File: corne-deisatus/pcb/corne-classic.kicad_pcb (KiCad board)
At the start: 2 copper layers, 147.2 x 94.7 mm, 101 parts, among them J1 MJ-4PP-9, J2 OLED, J3 LED, P1 i2c-pin, P2 i2c-pin, SW1 SW_PUSH, SW10 SW_PUSH, SW11 SW_PUSH, SW12 SW_PUSH, SW13 SW_PUSH, SW14 SW_PUSH, SW15 SW_PUSH, SW16 SW_PUSH, SW17 SW_PUSH, SW18 SW_PUSH, SW19 SW_PUSH, SW2 SW_PUSH, SW20 SW_PUSH, SW21 SW_PUSH, SW22 SW_PUSH, SW3 SW_PUSH, SW4 SW_PUSH, SW5 SW_PUSH, SW6 SW_PUSH, SW7 SW_PUSH, SW8 SW_PUSH, SW9 SW_PUSH, U1 ProMicro

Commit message: working on tracks
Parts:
- SW1, SW10, SW11, SW12, SW13, SW14, SW15, SW16, SW17, SW18, SW19, SW2, SW20, SW3, SW4, SW5, SW6, SW7, SW8, SW9: footprint kailh-pg1425-x-switch:MX-ALPS-Choc-X-straight-crane -> kailh-pg1425-x-switch:MX-ALPS-Choc-X-straight-crane2
- SW21, SW22: footprint kailh-pg1425-x-switch:MX-ALPS-Choc-X-straight-crane-u1.5 -> kailh-pg1425-x-switch:MX-ALPS-Choc-X-straight-crane2-u1.5
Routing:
- net GND: track 764.2 -> 76.1 mm, vias 43 -> 3
- net col1: track 221.3 -> 30.0 mm, vias 4 -> 2
- net col2: track 197.5 -> 17.9 mm, vias 8 -> 2
- net row0: track 205.5 -> 28.9 mm, vias 3 -> 0
- net col3: track 189.0 -> 17.6 mm, vias 6 -> 2
- net row1: track 191.7 -> 21.7 mm, vias 11 -> 0
- net col0: track 245.7 -> 95.9 mm, vias 4 -> 2
- net col4: track 161.0 -> 28.2 mm, vias 6 -> 2
- net Net-(L15-Pad3): track 77.2 -> 0.00 mm, vias 8 -> 0
- net col5: track 151.0 -> 77.2 mm, vias 2 -> 4
- net Net-(L14-Pad3): track 65.8 -> 0.00 mm, vias 8 -> 0
- net Net-(L4-Pad1): track 52.1 -> 0.00 mm, vias 5 -> 0
- net Net-(L2-Pad3): track 48.0 -> 0.00 mm, vias 3 -> 0
- net Net-(L1-Pad3): track 46.7 -> 0.00 mm, vias 3 -> 0
- net Net-(L5-Pad1): track 45.8 -> 0.00 mm, vias 3 -> 0
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- added copper zone on B.Cu, net GND

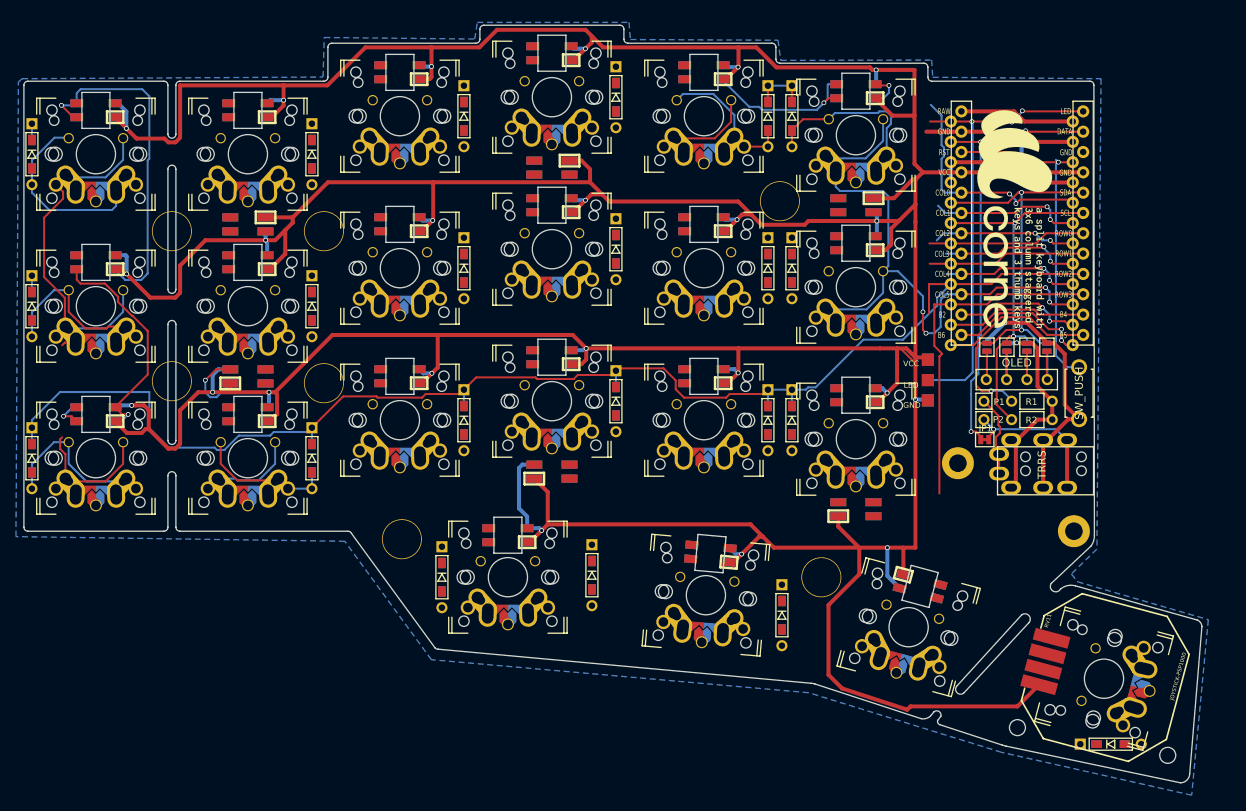
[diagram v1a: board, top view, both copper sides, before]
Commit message: adding tracks
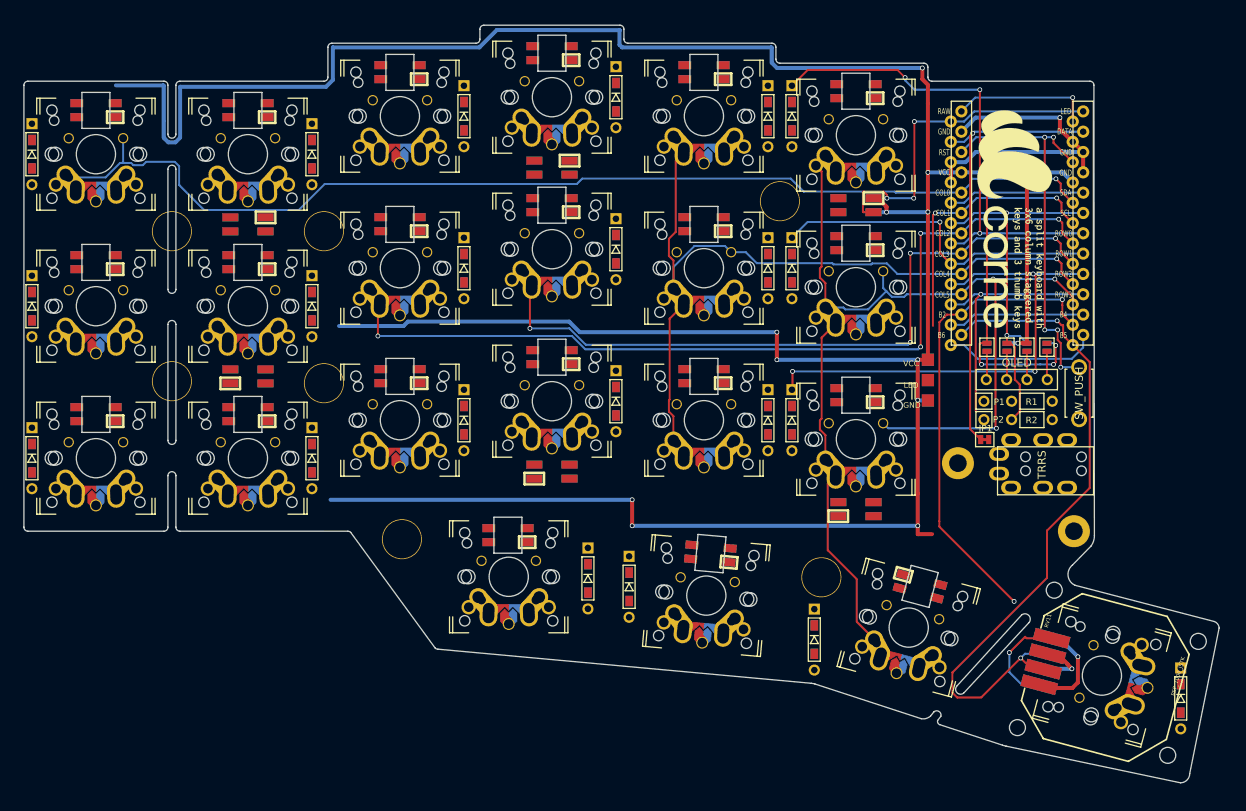
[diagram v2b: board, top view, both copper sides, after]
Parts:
- RV11: value JOYSTICK-PSP1000 -> PSP_1000_JSTK; footprint HackPack_Footprints:JOYSTICK-PSP1000 -> HackPack_Footprints:JOYSTICK-PSP1000-reverse
- SW20: footprint kailh-pg1425-x-switch:MX-ALPS-Choc-X-straight-crane2 -> kailh-pg1425-x-switch:MX-ALPS-Choc-X-straight-crane2-u1.5
- SW22: footprint kailh-pg1425-x-switch:MX-ALPS-Choc-X-straight-crane2-u1.5 -> kailh-pg1425-x-switch:MX-ALPS-Choc-X-straight-crane2
- moved SW19 75.5 mm to (121.6, 129.9), turned to 180 degrees
- moved D22 68.6 mm to (131.5, 130.2), turned to 270 degrees
- moved D21 50.9 mm to (205.6, 145.2)
- moved D20 28.9 mm to (159.8, 137.8)
- moved SW21 25.7 mm to (171.6, 136.3), turned to 165 degrees
- moved SW20 24.9 mm to (146.3, 132.3), turned to 175 degrees
- moved SW22 24.9 mm to (195.8, 142.3), turned to 255 degrees
- moved D19 23.4 mm to (136.7, 131.2)
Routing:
- net VCC: track 738.2 -> 404.4 mm, vias 24 -> 14
- net row2: track 172.1 -> 62.3 mm, vias 0 -> 3
- net col2: track 17.9 -> 108.6 mm, vias 2 -> 4
- net col3: track 17.6 -> 88.9 mm, vias 2 -> 4
- net analogY: track 17.5 -> 88.0 mm
- net col4: track 28.2 -> 94.0 mm, vias 2 -> 1
- net analogX: track 16.0 -> 72.7 mm, vias 2 -> 3
- net col5: track 77.2 -> 130.9 mm, vias 4 -> 3
- net col0: track 95.9 -> 138.6 mm, vias 2 -> 1
- net Net-(L13-Pad3): track 42.7 -> 0.00 mm, vias 1 -> 0
- net row0: track 28.9 -> 60.5 mm, vias 0 -> 3
- net Net-(L13-Pad1): track 28.5 -> 0.00 mm, vias 1 -> 0
- net Net-(D1-Pad2): track 28.3 -> 0.00 mm
- net GND: track 76.1 -> 48.2 mm, vias 3 -> 2
- net Net-(D6-Pad2): track 22.6 -> 0.00 mm
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- removed copper zone on B.Cu, net GND
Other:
- board size 147.2 x 94.7 mm -> 149.4 x 94.7 mm

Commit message: adding tracks
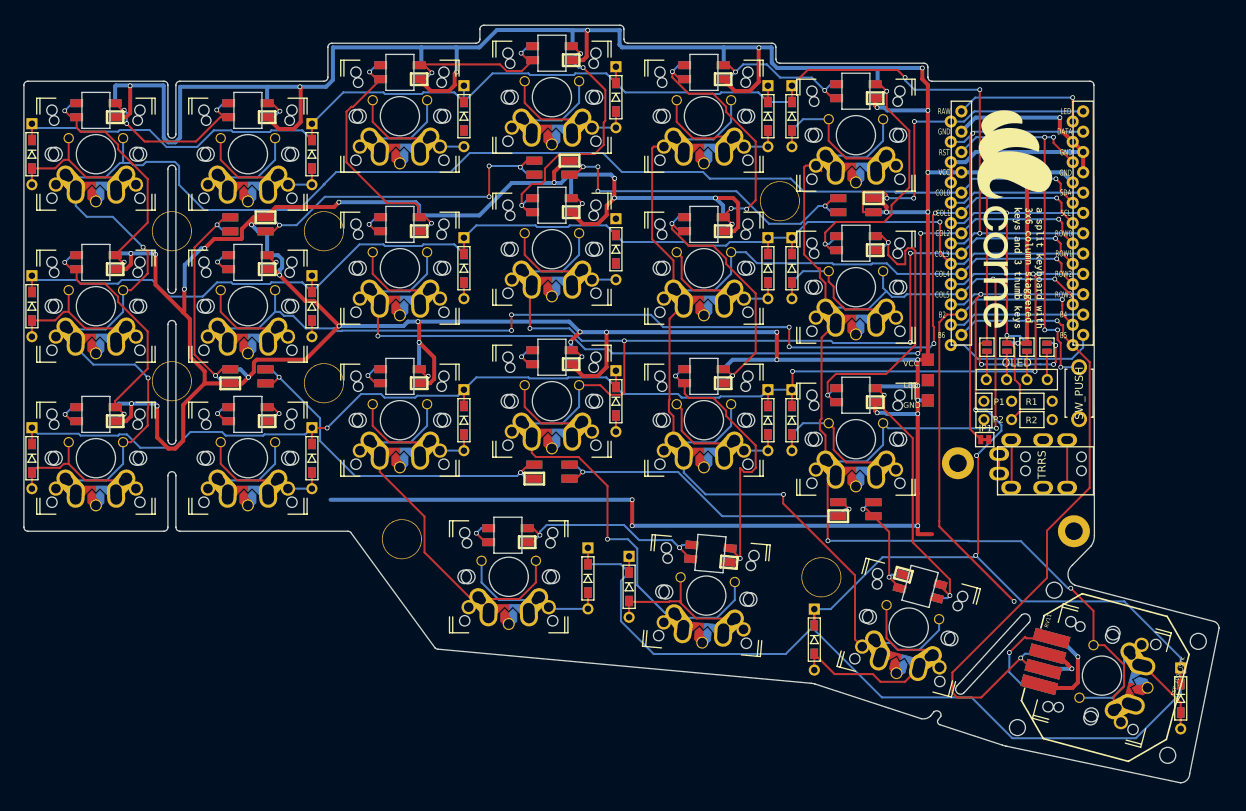
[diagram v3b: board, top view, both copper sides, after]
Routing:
- net VCC: track 404.4 -> 726.2 mm, vias 14 -> 44
- net row3: track 31.9 -> 214.1 mm, vias 1 -> 4
- net col1: track 34.1 -> 157.2 mm, vias 2 -> 7
- net row0: track 60.5 -> 176.2 mm
- net row2: track 62.3 -> 176.6 mm, vias 3 -> 4
- net row1: track 42.2 -> 155.6 mm
- net col3: track 88.9 -> 179.1 mm, vias 4 -> 6
- net col4: track 94.0 -> 166.4 mm, vias 1 -> 2
- net col2: track 108.6 -> 175.7 mm
- net col0: track 138.6 -> 203.9 mm, vias 1 -> 3
- net col5: track 130.9 -> 193.1 mm, vias 3 -> 5
- net Net-(L4-Pad1): track 0.00 -> 45.5 mm, vias 0 -> 2
- net Net-(L2-Pad3): track 0.77 -> 44.8 mm, vias 0 -> 4
- net Net-(L1-Pad3): track 0.00 -> 43.9 mm, vias 0 -> 4
- net Net-(L5-Pad1): track 0.00 -> 41.7 mm, vias 0 -> 2
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
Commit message: mostly done
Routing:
- net VCC: track 726.2 -> 809.8 mm, vias 44 -> 55
- net Net-(L15-Pad1): track 7.42 -> 32.4 mm
- net col1: track 157.2 -> 177.4 mm, vias 7 -> 8
- net analogX: track 72.7 -> 79.0 mm, vias 3 -> 5
- net Net-(L20-Pad3): track 7.65 -> 8.21 mm

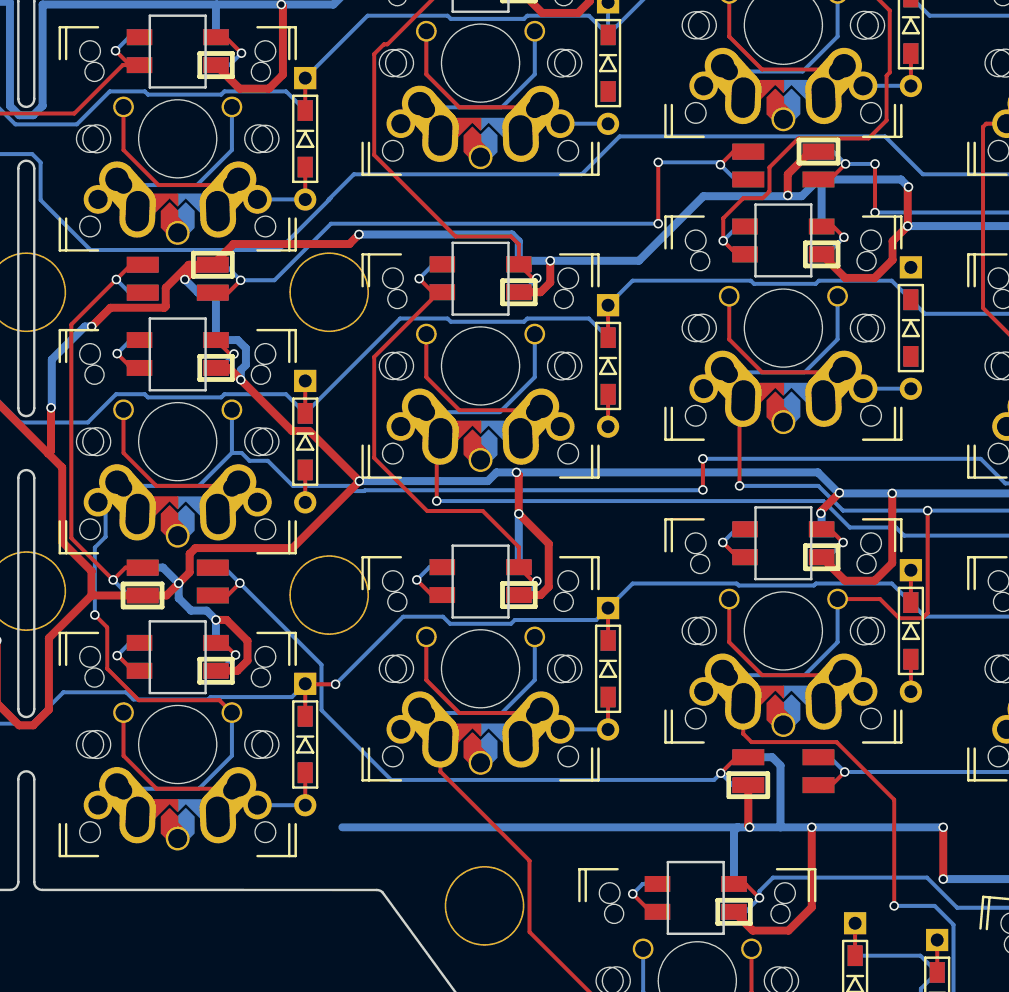
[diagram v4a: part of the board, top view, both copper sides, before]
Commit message: added all tracks except GND
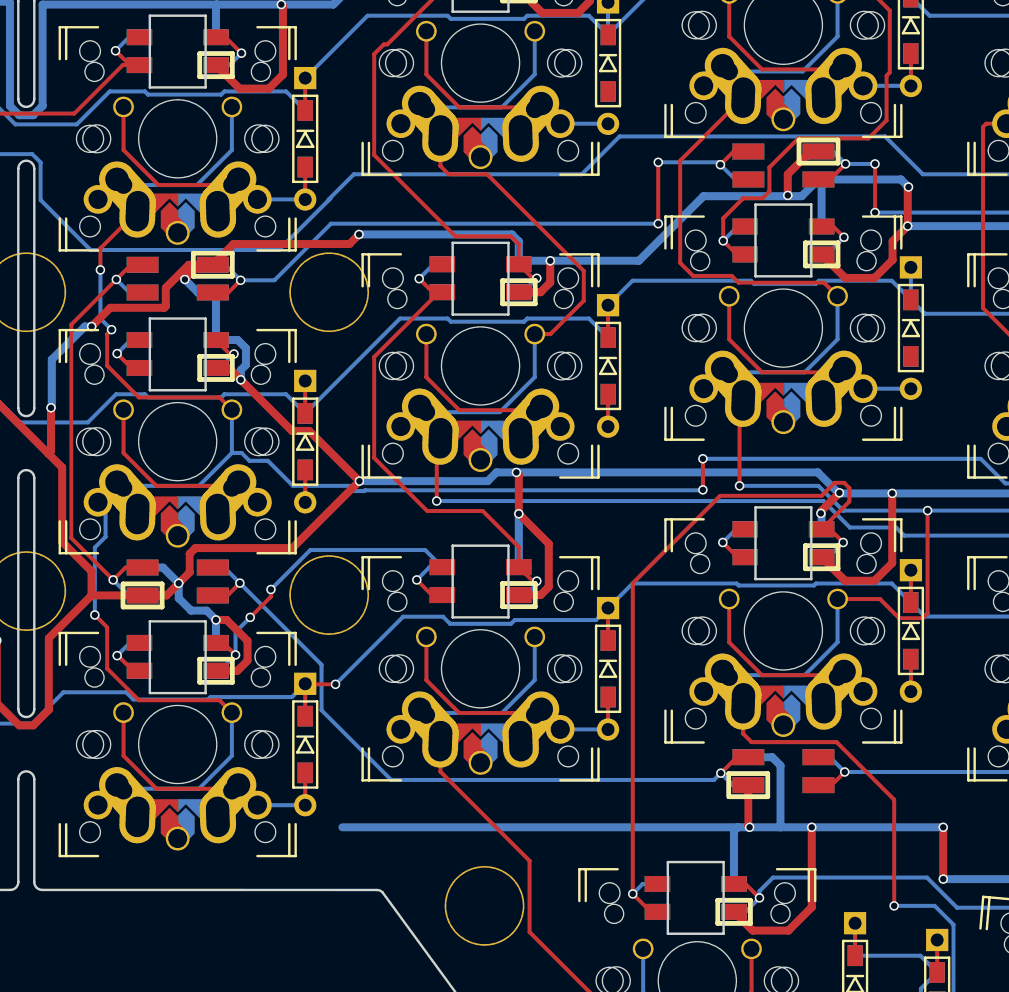
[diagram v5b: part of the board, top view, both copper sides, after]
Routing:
- net Net-(L22-Pad3): track 7.32 -> 46.5 mm
- net col3: track 179.1 -> 201.9 mm
- net col1: track 177.4 -> 197.5 mm, vias 8 -> 10
- net col2: track 175.7 -> 195.1 mm
- net Net-(L20-Pad3): track 8.21 -> 25.5 mm, vias 2 -> 4
- net row1: track 155.6 -> 157.6 mm

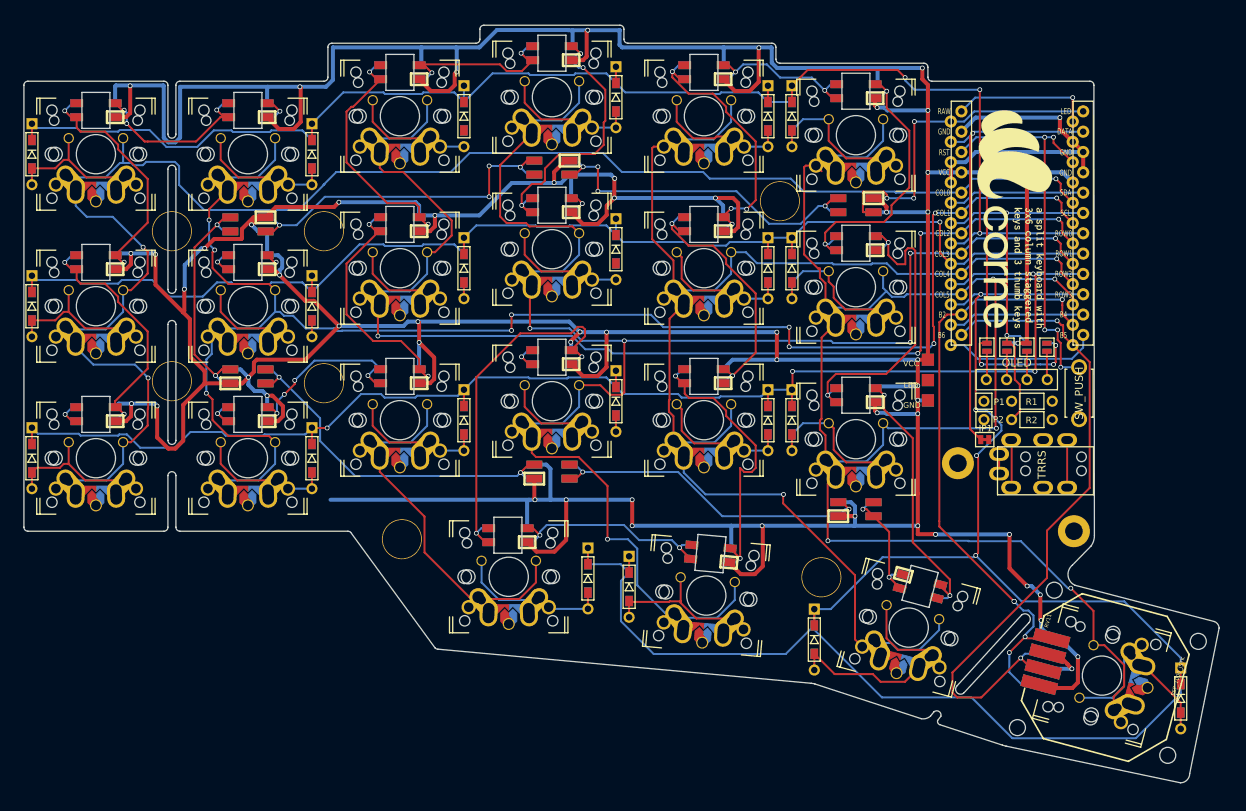
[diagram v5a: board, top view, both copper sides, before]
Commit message: added all tracks except GND
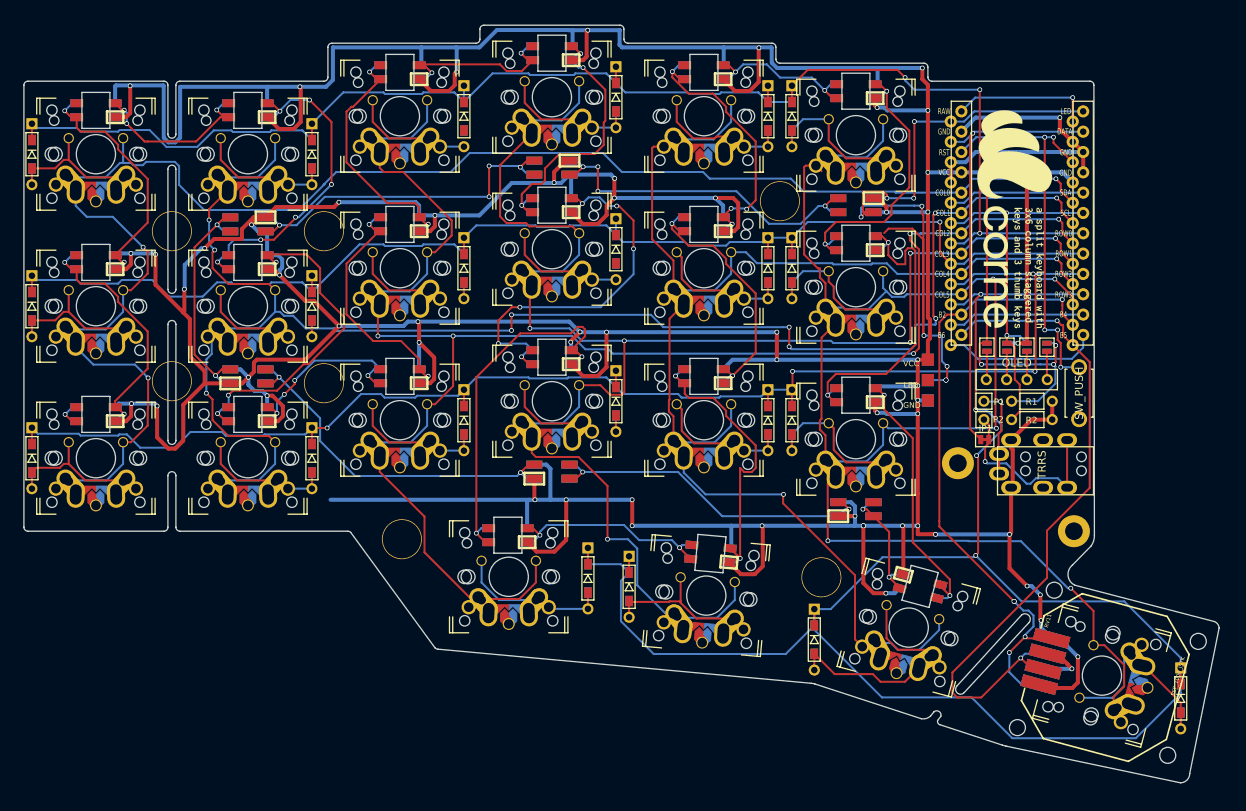
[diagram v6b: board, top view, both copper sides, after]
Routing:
- net LED: track 43.7 -> 98.8 mm, vias 3 -> 9
- net Net-(L16-Pad3): track 7.26 -> 48.7 mm, vias 2 -> 6
- net Net-(L14-Pad3): track 7.08 -> 42.7 mm, vias 2 -> 3
- net VCC: track 809.8 -> 843.6 mm, vias 55 -> 59
- net Net-(L14-Pad1): track 7.45 -> 40.8 mm, vias 2 -> 6
- net Net-(J1-PadB): track 5.95 -> 23.8 mm, vias 0 -> 1
- net col2: track 195.1 -> 207.2 mm, vias 4 -> 5
- net SDA: track 52.3 -> 61.3 mm
- net Net-(J1-PadA): track 2.45 -> 11.3 mm, vias 0 -> 1
- net col1: track 197.5 -> 198.6 mm

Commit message: all tracks done
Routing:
- net GND: track 48.2 -> 386.6 mm, vias 2 -> 82
- net VCC: track 843.6 -> 860.2 mm, vias 59 -> 62
- net Net-(L7-Pad3): track 24.0 -> 31.4 mm
- net col1: track 198.6 -> 205.8 mm
- net Net-(L14-Pad1): track 40.8 -> 47.2 mm, vias 6 -> 4
- net LED: track 98.8 -> 93.1 mm
- net Net-(L4-Pad1): track 45.5 -> 48.7 mm, vias 2 -> 3
- net Net-(D16-Pad2): track 12.9 -> 15.9 mm
- net Net-(D9-Pad2): track 12.9 -> 15.9 mm
- net Net-(D8-Pad2): track 12.9 -> 15.9 mm
- net col5: track 193.1 -> 190.2 mm
- net reset: track 49.8 -> 47.0 mm, vias 5 -> 3
- net Net-(L1-Pad1): track 29.6 -> 32.3 mm
- net Net-(U1-Pad12): track 19.4 -> 21.9 mm
- net Net-(L2-Pad3): track 44.8 -> 46.1 mm
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- added copper zone on B.Cu, net GND
- added copper zone on F.Cu, net GND

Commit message: every thing connected
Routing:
- net VCC: track 860.2 -> 869.9 mm
- net col4: track 166.4 -> 173.9 mm
- net col2: track 207.2 -> 214.4 mm
- net col3: track 201.9 -> 208.9 mm
- net col5: track 190.2 -> 195.5 mm
- net col1: track 205.8 -> 211.1 mm
- net col0: track 202.9 -> 208.2 mm
- net Net-(D3-Pad2): track 13.9 -> 17.7 mm
- net GND: track 386.6 -> 390.1 mm, vias 82 -> 86
- net Net-(D8-Pad2): track 15.9 -> 17.9 mm
- net Net-(D15-Pad2): track 15.9 -> 17.9 mm
- net Net-(D7-Pad2): track 17.9 -> 19.9 mm
- net Net-(D13-Pad2): track 17.9 -> 19.9 mm
- net Net-(D1-Pad2): track 17.9 -> 19.9 mm
- net Net-(D9-Pad2): track 15.9 -> 17.9 mm
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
